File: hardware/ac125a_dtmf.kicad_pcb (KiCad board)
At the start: 2 copper layers, 120 x 127 mm, 103 parts, among them J1 112-050-113R001, J2 Conn_01x06_Male, J3 USB_B, J4 DB9_Female_MountingHoles, SW1 SW_Push, U1 PIC18F4550-IP, U10 LAA108, U11 LAA108, U12 H11AA1, U13 H11AA1, U14 MAX202, U2 MT8870, U3 MT8870, U4 74HC595, U5 74HC595, U6 LAA108, U7 LAA108, U8 LAA108, U9 LAA108, Y1 3.579545MHZ

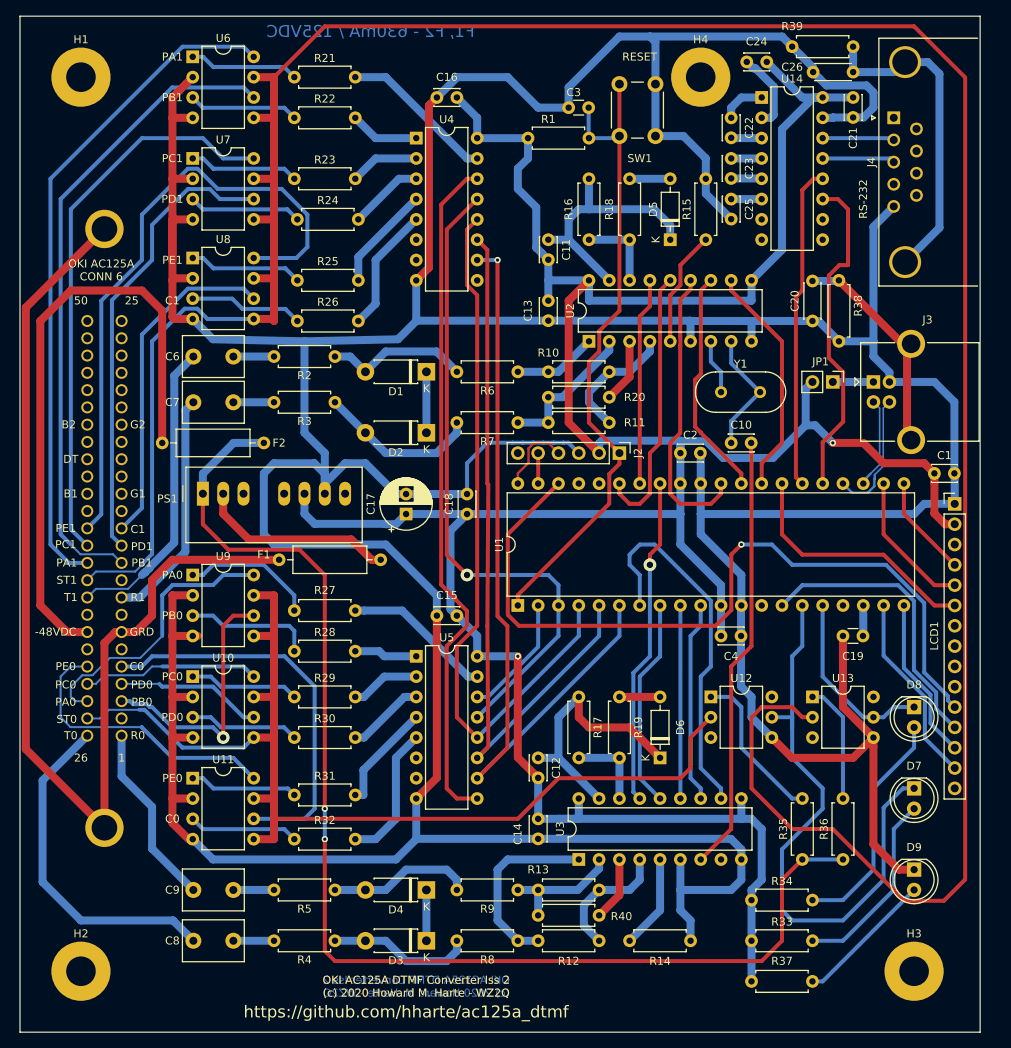
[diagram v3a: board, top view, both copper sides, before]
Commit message: Issue 3: Utilize we755a_dtmf boards.
     * Carrier for 2*we755a_dtmf boards.
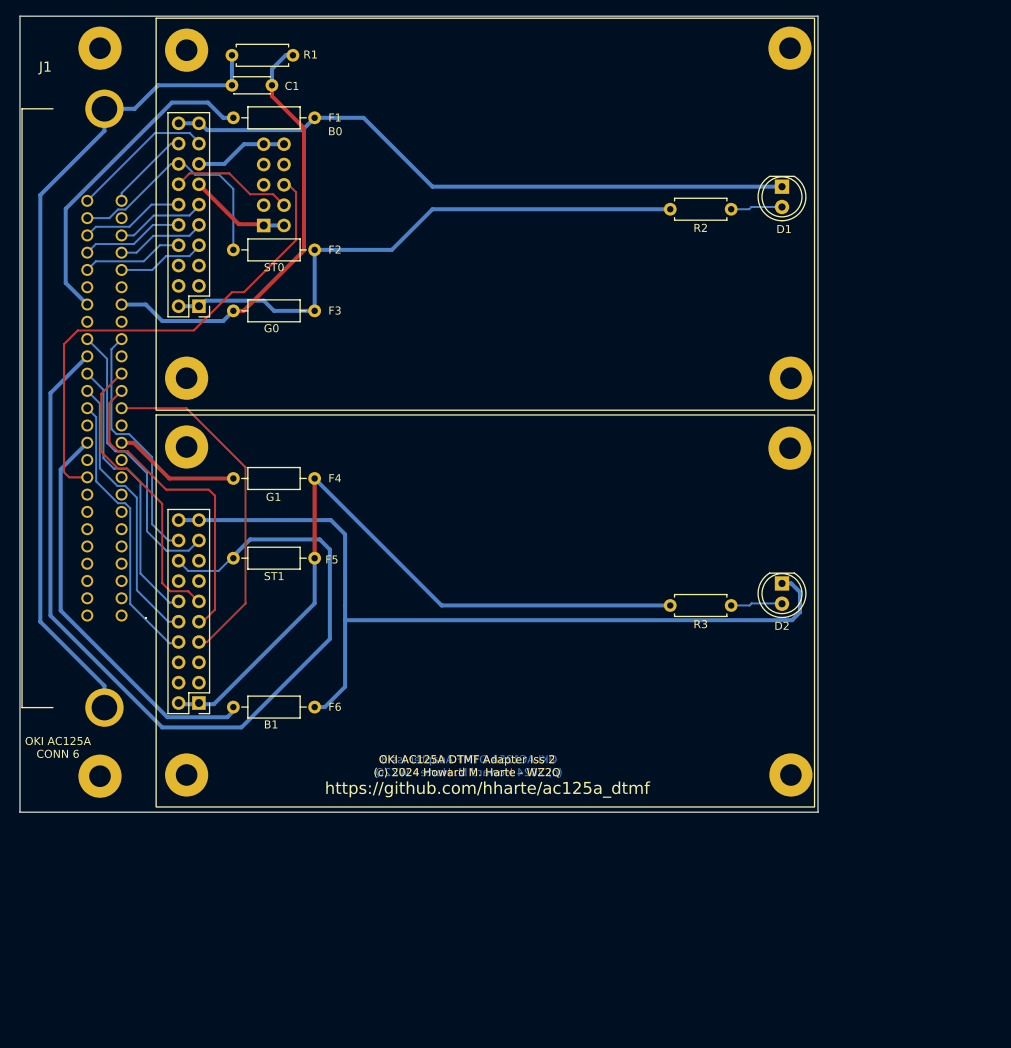
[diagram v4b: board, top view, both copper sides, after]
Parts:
- removed C10: 30pF, Capacitor_THT:C_Disc_D3.0mm_W2.0mm_P2.50mm
- removed C11, C12, C13, C14, C15, C16, C18, C2, C21, C22, C23, C24, C25, C4: 0.1uF, Capacitor_THT:C_Disc_D3.0mm_W2.0mm_P2.50mm
- removed C17: 10uF 25V, Capacitor_THT:CP_Radial_D6.3mm_P2.50mm
- removed C19: 0.47uF, Capacitor_THT:C_Disc_D3.0mm_W1.6mm_P2.50mm
- removed C20, C26: 4700pF, Capacitor_THT:C_Disc_D4.3mm_W1.9mm_P5.00mm
- removed C3: 0.01uF, Capacitor_THT:C_Disc_D3.0mm_W1.6mm_P2.50mm
- removed C6, C7, C8, C9: 0.01uF/630V, Capacitor_THT:C_Disc_D7.5mm_W5.0mm_P5.00mm
- removed D3, D4: 1N4734A, Diode_THT:D_DO-41_SOD81_P7.62mm_Horizontal
- removed D5, D6: 1N4148, Diode_THT:D_DO-35_SOD27_P7.62mm_Horizontal
- removed D7, D8, D9: LED, LED_THT:LED_D5.0mm
- removed JP1: VUSB, Connector_PinHeader_2.54mm:PinHeader_1x02_P2.54mm_Vertical
- removed LCD1: DMC-16105-LY, Connector_PinHeader_2.54mm:PinHeader_1x15_P2.54mm_Vertical
- removed PS1: SPBW06, Converter_DCDC:Converter_DCDC_TRACO_TMR-xxxx_THT
- removed R10, R12: 52.3K 1%, Resistor_THT:R_Axial_DIN0207_L6.3mm_D2.5mm_P7.62mm_Horizontal
- removed R11, R13: 68.1K 1%, Resistor_THT:R_Axial_DIN0207_L6.3mm_D2.5mm_P7.62mm_Horizontal
- removed R14, R15: 10K, Resistor_THT:R_Axial_DIN0207_L6.3mm_D2.5mm_P7.62mm_Horizontal
- removed R16, R17: 330K, Resistor_THT:R_Axial_DIN0207_L6.3mm_D2.5mm_P7.62mm_Horizontal
- removed R18, R19: 100K, Resistor_THT:R_Axial_DIN0207_L6.3mm_D2.5mm_P7.62mm_Horizontal
- removed R20, R40: 220K 1%, Resistor_THT:R_Axial_DIN0207_L6.3mm_D2.5mm_P7.62mm_Horizontal
- removed R21, R22, R23, R24, R25, R26, R27, R28, R29, R30, R31, R32, R33, R34: 220, Resistor_THT:R_Axial_DIN0207_L6.3mm_D2.5mm_P7.62mm_Horizontal
- removed R35, R36: 2.7K, Resistor_THT:R_Axial_DIN0207_L6.3mm_D2.5mm_P7.62mm_Horizontal
- removed R37: 470, Resistor_THT:R_Axial_DIN0207_L6.3mm_D2.5mm_P7.62mm_Horizontal
- removed R38, R39: 1M, Resistor_THT:R_Axial_DIN0207_L6.3mm_D2.5mm_P7.62mm_Horizontal
- removed R4, R5: 110K 1% 1W, Resistor_THT:R_Axial_DIN0207_L6.3mm_D2.5mm_P7.62mm_Horizontal
- removed R6, R7, R8, R9: 110K 1%, Resistor_THT:R_Axial_DIN0207_L6.3mm_D2.5mm_P7.62mm_Horizontal
- removed SW1: SW_Push, Button_Switch_THT:SW_PUSH_6mm
- removed U1: PIC18F4550-IP, Package_DIP:DIP-40_W15.24mm
- removed U10, U11, U6, U7, U8, U9: LAA108, Package_DIP:DIP-8_W7.62mm
- removed U12, U13: H11AA1, Package_DIP:DIP-6_W7.62mm
- removed U14: MAX202, Package_DIP:DIP-16_W7.62mm
- removed U2, U3: MT8870, Package_DIP:DIP-18_W7.62mm
- removed U4, U5: 74HC595, Package_DIP:DIP-16_W7.62mm
- removed Y1: 3.579545MHZ, Crystal:Crystal_HC49-U_Vertical
- added F3: Fuse 500mA, Resistor_THT:R_Axial_DIN0207_L6.3mm_D2.5mm_P10.16mm_Horizontal, F.Cu at (59.7, 63.5)
- added F4: Fuse 500mA, Resistor_THT:R_Axial_DIN0207_L6.3mm_D2.5mm_P10.16mm_Horizontal, F.Cu at (59.7, 84.5)
- added F5: Fuse 500mA, Resistor_THT:R_Axial_DIN0207_L6.3mm_D2.5mm_P10.16mm_Horizontal, F.Cu at (69.8, 94.4)
- added F6: Fuse 500mA, Resistor_THT:R_Axial_DIN0207_L6.3mm_D2.5mm_P10.16mm_Horizontal, F.Cu at (69.8, 113.0)
- C1: value 0.1uF -> 4700pF; footprint Capacitor_THT:C_Disc_D3.0mm_W2.0mm_P2.50mm -> Capacitor_THT:C_Disc_D4.3mm_W1.9mm_P5.00mm
- D1, D2: value 1N4734A -> LED; footprint Diode_THT:D_DO-41_SOD81_P7.62mm_Horizontal -> LED_THT:LED_D5.0mm
- F1, F2: value Fuse 630mA -> Fuse 500mA; footprint Resistor_THT:R_Axial_DIN0309_L9.0mm_D3.2mm_P12.70mm_Horizontal -> Resistor_THT:R_Axial_DIN0207_L6.3mm_D2.5mm_P10.16mm_Horizontal
- H1, H2, H3, H4: footprint MountingHole:MountingHole_3.7mm_Pad -> MountingHole:MountingHole_2.7mm_Pad
- J1: moved to F.Cu
- J2: value Conn_01x06_Male -> Conn_02x10_Odd_Even; footprint Connector_PinHeader_2.54mm:PinHeader_1x06_P2.54mm_Vertical -> ac125a_dtmf:WE755A-DTMF
- J3: value USB_B -> Conn_02x10_Odd_Even; footprint Connector_USB:USB_B_OST_USB-B1HSxx_Horizontal -> ac125a_dtmf:WE755A-DTMF
- J4: value DB9_Female_MountingHoles -> Conn_02x05_Odd_Even; footprint Connector_Dsub:DSUB-9_Female_Horizontal_P2.77x2.84mm_EdgePinOffset7.70mm_Housed_MountingHolesOffset9.12mm -> Connector_PinHeader_2.54mm:PinHeader_2x05_P2.54mm_Vertical; moved to B.Cu
- R1: value 4.7K -> 1M
- R2, R3: value 110K 1% 1W -> 10K
- moved H2 145.5 mm to (129.3, 30.7)
- moved H4 115.2 mm to (43.0, 121.7)
- moved C1 100.3 mm to (59.5, 35.3)
- moved J3 92.5 mm to (56.4, 112.5)
- moved J4 79.9 mm to (63.5, 52.8), turned to 0 degrees
- moved H3 67.2 mm to (129.3, 80.7)
- moved R3 55.7 mm to (121.9, 100.3)
- moved F1 55.4 mm to (69.8, 39.4), turned to 180 degrees
- moved J2 54.7 mm to (56.4, 62.9), turned to 0 degrees
- moved R2 52.8 mm to (121.9, 50.8)
- moved D1 50.1 mm to (128.3, 48.0), turned to -90 degrees
- moved D2 48.3 mm to (128.3, 97.6), turned to -90 degrees
- moved R1 38.4 mm to (59.5, 31.6)
- moved J1 36.8 mm to (45.7, 101.6), turned to -90 degrees
- moved F2 25.0 mm to (69.8, 55.9)
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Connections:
- C1 pad 1: +5V -> /SHIELD
- C1 pad 2: GND -> /G0
- D1 pad 1: Net-(D1-Pad1) -> /AC125A_B0
- D2 pad 1: Net-(D1-Pad1) -> /AC125A_B1
- F1 pad 1: Net-(F1-Pad1) -> /AC125A_B0
- F1 pad 2: /AC125A_G0 -> /B0
- F2 pad 1: /AC125A_B0 -> /AC125A_G0
- F2 pad 2: Net-(F2-Pad2) -> /AC125A_ST0
- J1 pad 15: /AC125A_G1 -> /G1
- J1 pad 32: Net-(F2-Pad2) -> /B0
- J1 pad 40: /AC125A_B1 -> /B1
- J1 pad 7: Net-(F1-Pad1) -> /G0
- J1 pad MH1: Net-(F1-Pad1) -> /SHIELD
- J1 pad MH2: Net-(F1-Pad1) -> /SHIELD
- J2 pad 1: /Microcontroller/MCLR -> /AC125A_G0
- J2 pad 2: +5V -> /AC125A_G0
- J2 pad 3: GND -> /LINK_SPARE
- J2 pad 4: /Microcontroller/ICSP_PGD -> /LINK_C1
- J2 pad 5: /Microcontroller/ICSP_PGC -> /LINK_6
- J2 pad 6: unconnected-(J2-Pad6) -> /LINK_5-6
- J3 pad 1: Net-(J3-Pad1) -> /AC125A_G1
- J3 pad 2: /Microcontroller/USB_D- -> /AC125A_G1
- J3 pad 3: /Microcontroller/USB_D+ -> unconnected-(J3-Pin_3-Pad3)
- J3 pad 4: GND -> unconnected-(J3-Pin_4-Pad4)
- J3 pad 5: Net-(C20-Pad2) -> unconnected-(J3-Pin_5-Pad5)
- J4 pad 1: unconnected-(J4-Pad1) -> GND
- J4 pad 2: Net-(J4-Pad2) -> GND
- J4 pad 3: Net-(J4-Pad3) -> unconnected-(J4-Pin_3-Pad3)
- J4 pad 4: unconnected-(J4-Pad4) -> Net-(J2-Pin_14)
- J4 pad 5: GND -> unconnected-(J4-Pin_5-Pad5)
- J4 pad 6: unconnected-(J4-Pad6) -> /AC125A_DT
- J4 pad 9: unconnected-(J4-Pad9) -> +5V
- R1 pad 1: +5V -> /SHIELD
- R1 pad 2: /Microcontroller/MCLR -> /G0
- R2 pad 2: Net-(C6-Pad1) -> /AC125A_G0
- R3 pad 2: Net-(C7-Pad1) -> /AC125A_G1
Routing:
- net GND: track 724.0 -> 12.8 mm
- net +5V: track 372.4 -> 11.7 mm, vias 2 -> 0
- net /AC125A_ST1: track 345.1 -> 112.2 mm
- net /AC125A_ST0: track 184.8 -> 30.1 mm
- net Net-(F1-Pad1): track 134.8 -> 0.00 mm
- net /AC125A_B1: track 0.00 -> 107.9 mm
- net /SHIELD: track 0.00 -> 102.4 mm
- net /Microcontroller/SSR_SRCLR_: track 98.3 -> 0.00 mm, vias 1 -> 0
- net /Microcontroller/LCD_DB4: track 97.5 -> 0.00 mm, vias 1 -> 0
- net /Microcontroller/SSR_SRCLK: track 91.3 -> 0.00 mm
- net /Microcontroller/SSR_RCLK: track 89.7 -> 0.00 mm
- net /AC125A_G1: track 0.00 -> 88.3 mm
- net /Microcontroller/SSR Drivers/SR_OUT: track 85.5 -> 0.00 mm
- net /Microcontroller/SSR_OE_: track 82.3 -> 0.00 mm, vias 1 -> 0
- net /Microcontroller/MCLR: track 81.3 -> 0.00 mm
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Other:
- board size 120 x 127 mm -> 99.8 x 99.5 mm
- board text added: "AC125A - OR0"
- board text added: "AC125A - OR1"
- board text added: "B0"
- board text added: "G0"
- board text added: "OKI AC125A DTMF Adapter Iss 2 (c) 2024 Howard M. Harte - WZ2Q"
- board text added: "OKI AC125A DTMF Adapter Iss 3 (c) 2024 Howard M. Harte - WZ2Q"
- board text removed: "-48VDC"
- board text removed: "F1, F2 - 630mA / 125VDC"
- board text removed: "GRD"
- board text removed: "Install RJ21X Connector on solder side."
- board text removed: "OKI AC125A DTMF Converter Iss 2 (c) 2020 Howard M. Harte - WZ2Q"
- board text removed: "RESET"
- board text removed: "RS-232"
